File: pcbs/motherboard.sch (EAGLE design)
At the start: 33 parts, among them U1 DRV8302DCAR, U2 TEENSY3.2, U3 PSOC5LP, U4 IRF7749L, U5 IRF7749L, U6 IRF7749L, U7\ IRF7749L, U8 IRF7749L, U9 IRF7749L

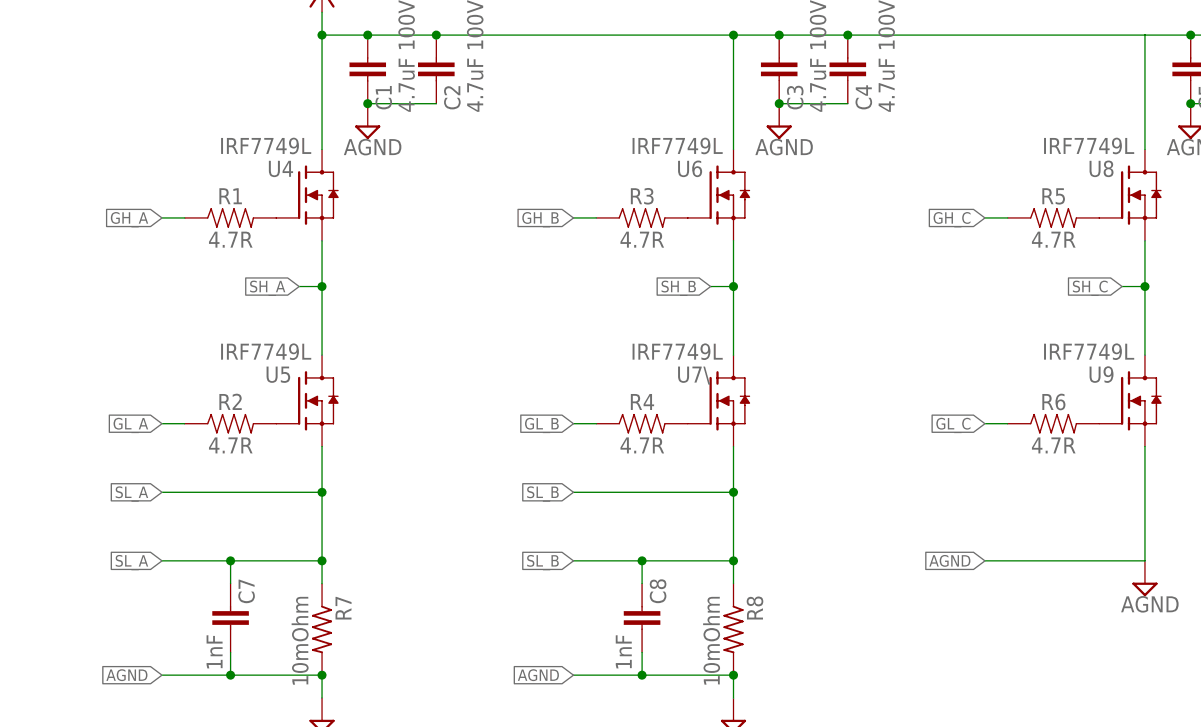
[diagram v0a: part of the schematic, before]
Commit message: Laid out single FET stage
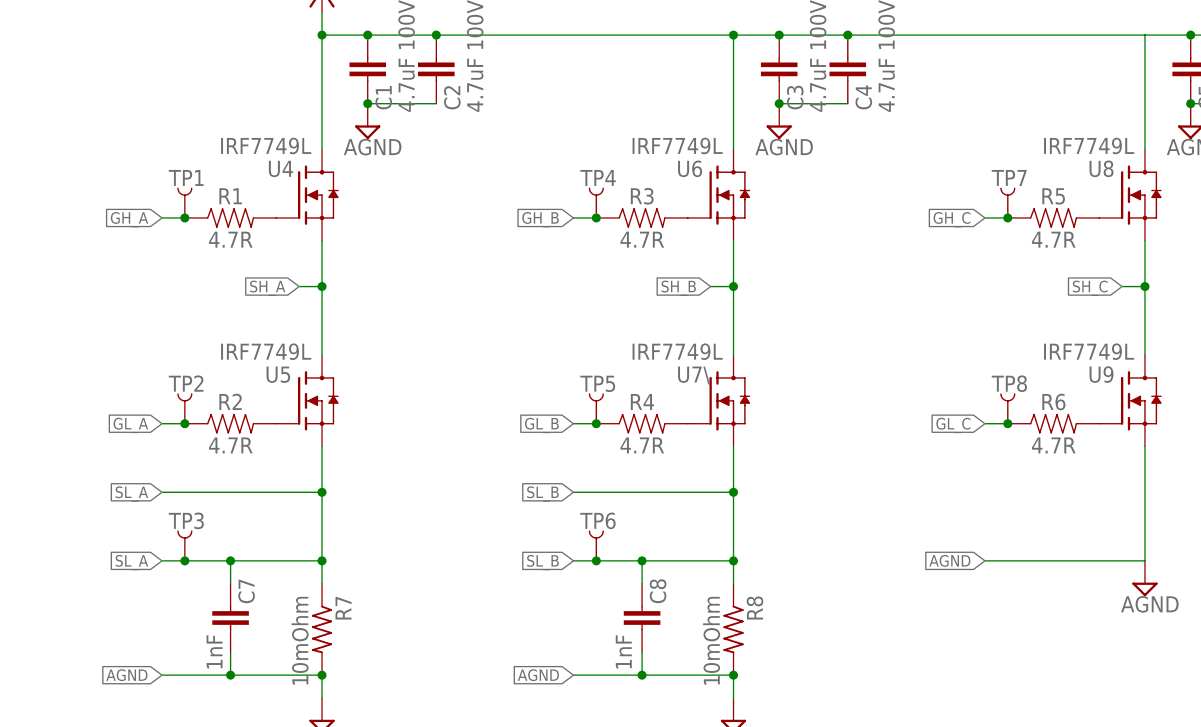
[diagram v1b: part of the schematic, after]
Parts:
- added TP1, TP2, TP3, TP4, TP5, TP6, TP7, TP8: TEST-POINT3, SparkFun-Connectors:TEST-POINT3
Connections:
- net GH_A: now also TP1.1
- net GH_B: now also TP4.1
- net GH_C: now also TP7.1
- net GL_A: now also TP2.1
- net GL_B: now also TP5.1
- net GL_C: now also TP8.1
- net SL_A: now also TP3.1
- net SL_B: now also TP6.1
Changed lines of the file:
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@@
 <part name="SUPPLY11" library="supply2" library_urn="urn:adsk.eagle:library:372" deviceset="DGND" device=""/>
 <part name="SUPPLY12" library="supply2" library_urn="urn:adsk.eagle:library:372" deviceset="DGND" device=""/>
+<part name="TP1" library="SparkFun-Connectors" deviceset="TEST-POINT" device="3"/>
+<part name="TP2" library="SparkFun-Connectors" deviceset="TEST-POINT" device="3"/>
+<part name="TP3" library="SparkFun-Connectors" deviceset="TEST-POINT" device="3"/>
+<part name="TP4" library="SparkFun-Connectors" deviceset="TEST-POINT" device="3"/>
+<part name="TP5" library="SparkFun-Connectors" deviceset="TEST-POINT" device="3"/>
+<part name="TP6" library="SparkFun-Connectors" deviceset="TEST-POINT" device="3"/>
+<part name="TP7" library="SparkFun-Connectors" deviceset="TEST-POINT" device="3"/>
+<part name="TP8" library="SparkFun-Connectors" deviceset="TEST-POINT" device="3"/>
 </parts>
 <sheets>
@@
 <instance part="SUPPLY12" gate="G$1" x="-78.74" y="144.78" smashed="yes" rot="R180">
 <attribute name="VALUE" x="-76.073" y="147.955" size="1.778" layer="96" rot="R180"/>
+</instance>
+<instance part="TP1" gate="G$1" x="81.28" y="99.06" smashed="yes" rot="R90">
+<attribute name="NAME" x="79.502" y="102.616" size="1.778" layer="95" font="vector"/>
+</instance>
+<instance part="TP2" gate="G$1" x="81.28" y="76.2" smashed="yes" rot="R90">
+<attribute name="NAME" x="79.502" y="79.756" size="1.778" layer="95" font="vector"/>
+</instance>
+<instance part="TP3" gate="G$1" x="81.28" y="60.96" smashed="yes" rot="R90">
+<attribute name="NAME" x="79.502" y="64.516" size="1.778" layer="95" font="vector"/>
+</instance>
+<instance part="TP4" gate="G$1" x="127" y="99.06" smashed="yes" rot="R90">
+<attribute name="NAME" x="125.222" y="102.616" size="1.778" layer="95" font="vector"/>
+</instance>
+<instance part="TP5" gate="G$1" x="127" y="76.2" smashed="yes" rot="R90">
+<attribute name="NAME" x="125.222" y="79.756" size="1.778" layer="95" font="vector"/>
+</instance>
+<instance part="TP6" gate="G$1" x="127" y="60.96" smashed="yes" rot="R90">
+<attribute name="NAME" x="125.222" y="64.516" size="1.778" layer="95" font="vector"/>
+</instance>
+<instance part="TP7" gate="G$1" x="172.72" y="99.06" smashed="yes" rot="R90">
+<attribute name="NAME" x="170.942" y="102.616" size="1.778" layer="95" font="vector"/>
+</instance>
+<instance part="TP8" gate="G$1" x="172.72" y="76.2" smashed="yes" rot="R90">
+<attribute name="NAME" x="170.942" y="79.756" size="1.778" layer="95" font="vector"/>
 </instance>
 </instances>
@@
 <wire x1="81.28" y1="99.06" x2="78.74" y2="99.06" width="0.1524" layer="91"/>
 <label x="78.74" y="99.06" size="1.27" layer="95" rot="R180" xref="yes"/>
+<pinref part="TP1" gate="G$1" pin="1"/>
+<junction x="81.28" y="99.06"/>
 </segment>
 <segment>
@@
 <wire x1="81.28" y1="76.2" x2="78.74" y2="76.2" width="0.1524" layer="91"/>
 <label x="78.74" y="76.2" size="1.27" layer="95" rot="R180" xref="yes"/>
+<pinref part="TP2" gate="G$1" pin="1"/>
+<junction x="81.28" y="76.2"/>
 </segment>
 <segment>
@@
 <wire x1="127" y1="99.06" x2="124.46" y2="99.06" width="0.1524" layer="91"/>
 <label x="124.46" y="99.06" size="1.27" layer="95" rot="R180" xref="yes"/>
+<pinref part="TP4" gate="G$1" pin="1"/>
+<junction x="127" y="99.06"/>
 </segment>
 <segment>
@@
 <wire x1="127" y1="76.2" x2="124.46" y2="76.2" width="0.1524" layer="91"/>
 <label x="124.46" y="76.2" size="1.27" layer="95" rot="R180" xref="yes"/>
+<pinref part="TP5" gate="G$1" pin="1"/>
+<junction x="127" y="76.2"/>
 </segment>
 <segment>
@@
 <wire x1="172.72" y1="99.06" x2="170.18" y2="99.06" width="0.1524" layer="91"/>
 <label x="170.18" y="99.06" size="1.27" layer="95" rot="R180" xref="yes"/>
+<pinref part="TP7" gate="G$1" pin="1"/>
+<junction x="172.72" y="99.06"/>
 </segment>
 <segment>
@@
 <wire x1="172.72" y1="76.2" x2="170.18" y2="76.2" width="0.1524" layer="91"/>
 <label x="170.18" y="76.2" size="1.27" layer="95" rot="R180" xref="yes"/>
+<pinref part="TP8" gate="G$1" pin="1"/>
+<junction x="172.72" y="76.2"/>
 </segment>
 <segment>
@@
 <wire x1="86.36" y1="60.96" x2="96.52" y2="60.96" width="0.1524" layer="91"/>
 <junction x="96.52" y="60.96"/>
-<wire x1="86.36" y1="60.96" x2="78.74" y2="60.96" width="0.1524" layer="91"/>
+<wire x1="86.36" y1="60.96" x2="81.28" y2="60.96" width="0.1524" layer="91"/>
 <junction x="86.36" y="60.96"/>
 <label x="78.74" y="60.96" size="1.27" layer="95" rot="R180" xref="yes"/>
+<wire x1="81.28" y1="60.96" x2="78.74" y2="60.96" width="0.1524" layer="91"/>
 <wire x1="96.52" y1="68.58" x2="78.74" y2="68.58" width="0.1524" layer="91"/>
 <junction x="96.52" y="68.58"/>
 <label x="78.74" y="68.58" size="1.27" layer="95" rot="R180" xref="yes"/>
+<pinref part="TP3" gate="G$1" pin="1"/>
+<junction x="81.28" y="60.96"/>
 </segment>
 </net>
@@
 <wire x1="132.08" y1="60.96" x2="142.24" y2="60.96" width="0.1524" layer="91"/>
 <junction x="142.24" y="60.96"/>
-<wire x1="132.08" y1="60.96" x2="124.46" y2="60.96" width="0.1524" layer="91"/>
+<wire x1="132.08" y1="60.96" x2="127" y2="60.96" width="0.1524" layer="91"/>
 <junction x="132.08" y="60.96"/>
 <label x="124.46" y="60.96" size="1.27" layer="95" rot="R180" xref="yes"/>
+<wire x1="127" y1="60.96" x2="124.46" y2="60.96" width="0.1524" layer="91"/>
 <wire x1="142.24" y1="68.58" x2="124.46" y2="68.58" width="0.1524" layer="91"/>
 <junction x="142.24" y="68.58"/>
 <label x="124.46" y="68.58" size="1.27" layer="95" rot="R180" xref="yes"/>
-</segment>
-</net>
+<pinref part="TP6" gate="G$1" pin="1"/>
+<junction x="127" y="60.96"/>
+</segment>
+</net>

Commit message: Cleaned up eagle directory, laid out more of power stage
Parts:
- added C10: 120pF, SparkFun-Capacitors:100PF-0603-50V-5%
- added C11, C12, C14: 2.2uF, SparkFun-Capacitors:2.2UF-0805-25V-(+80/-20%)
- added C13: 22nF 36V, SparkFun-Capacitors:22NF/22,000PF-0603-50V-10%
- added C15, C17, C23: 4.7uF, SparkFun-Capacitors:4.7UF-0603-35V-(20%)
- added C16, C18, C19, C20, C21, C22, C24: 0.1uF, SparkFun-Capacitors:0.1UF-0603-25V-(+80/-20%)
- added C25: 100uF, SparkFun-Retired:100UF6.3V20%(1210)
- added C26: 15nF, SparkFun-Capacitors:10NF-0603-50V-10%
- added C9: 6.8nF, SparkFun-Capacitors:100PF-0603-50V-5%
- added D1: NRVBA2H100T3G, SparkFun-DiscreteSemi:DIODE-SCHOTTKY-SS14
- added IMU: SSM-104-L-SV, kanzi:SSM-104-L-SV
- added JP1, JP2, JP3, JP4, JP5: JUMPER-SMT_2_NC_TRACE_NO-SILK, SparkFun-Jumpers:JUMPER-SMT_2_NC_TRACE_NO-SILK
- added L1: 22uH, IndividualNode:LQH43MN330J03L
- added R15: 200k, SparkFun-Resistors:200KOHM-0603-1/10W-1%
- added R16: 16.2k, SparkFun-Resistors:16.2KOHM-0603-1/10W-1%
- added R17, R18, R19, R20, R21: 10k, SparkFun-Resistors:10KOHM-0603-1/10W-1%
- added R22: OPEN, SparkFun-Resistors:10KOHM-0603-1/10W-1%
- added R23: SHORT, SparkFun-Resistors:10KOHM-0603-1/10W-1%
- added R24: 1M, SparkFun-Resistors:1MOHM-0603-1/4W-5%
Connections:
- new net +3V3: IMU.3, U2.3V3
- new net ENABLE: U1.EN_GATE, U2.13
- new net LEFT_DC_CAL: U1.DC_CAL
- new net LEFT_FAULT: R19.1, U1.NFAULT, U2.22
- new net LEFT_OCTW: R20.1, U1.NOCTW, U2.23
- new net LEFT_SO1: U1.SO1, U2.17
- new net LEFT_SO2: U1.SO2, U2.16
- new net N$1: R15.1, U1.RT_CLK
- new net N$10: R17.2, R18.1, U1.VSENSE
- new net N$11: R22.1, R23.2, U1.OC_ADJ
- new net N$12: C11.1, C12.1, U1.GVDD
- new net N$13: R21.2, U1.DTC
- new net N$14: R23.1, U1.DVDD
- new net N$15: C13.1, U1.CP1
- new net N$16: C13.2, U1.CP2
- new net N$17: C14.1, U1.AVDD
- new net N$18: C15.1, C16.1, U1.PVDD1
- new net N$19: C17.1, C18.1, U1.PVDD2
- new net N$2: C9.2, R16.2
- new net N$20: C19.2, U1.BST_C
- new net N$21: C20.2, U1.BST_B
- new net N$22: C21.2, U1.BST_A
- new net N$23: R24.1, U1.BIAS
- new net N$24: C22.2, U1.BST_BK
- new net N$25: C22.1, D1.C, L1.1, U1.PH
- new net N$26: C23.1, C24.1, C25.1, L1.2
- new net N$27: C26.2, U1.SS_TR
- new net N$3: C10.2, R16.1, U1.COMP
- new net RIGHT_FAULT: U2.20
- new net RIGHT_OCTW: U2.21
- new net RIGHT_SO1: U2.15
- new net RIGHT_SO2: U2.14
- new net SCL: IMU.1, U2.19
- new net SDA: IMU.2, U2.18
- net +5V: now also R18.2, R19.2, R20.2, R22.2, U1.GAIN, U1.M_OC, U1.REF, U2.VIN
- net AGND: now also JP2.2, JP4.2, JP5.2
- net DGND: now also C10.1, C11.2, C12.2, C14.2, C15.2, C16.2, C17.2, C18.2, C23.2, C24.2, C25.2, C26.1, C9.1, D1.A, IMU.4, R15.2, R17.1, R21.1, R24.2, U1.AGND, U1.M_PWM, U1.PWR_PAD
- net LEFT_DIR: now also U2.7
- net LEFT_PWM: now also U2.5
- net RIGHT_DIR: now also U2.8
- net RIGHT_PWM: now also U2.6
- net SH_A: now also C21.1
- net SH_B: now also C20.1
- net SH_C: now also C19.1
- net SL_A: now also JP1.2
- net SL_B: now also JP3.2
- net SL_C: now also JP5.1
- net SN1: now also JP1.1
- net SN2: now also JP3.1
- net SP1: now also JP2.1
- net SP2: now also JP4.1
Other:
- moved on the sheet: LEFT_HALL, R10, R11, R12, R13, R14, R9, RIGHT_HALL, TP3, TP6, U1, U2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
